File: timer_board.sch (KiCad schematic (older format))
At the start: 17 parts

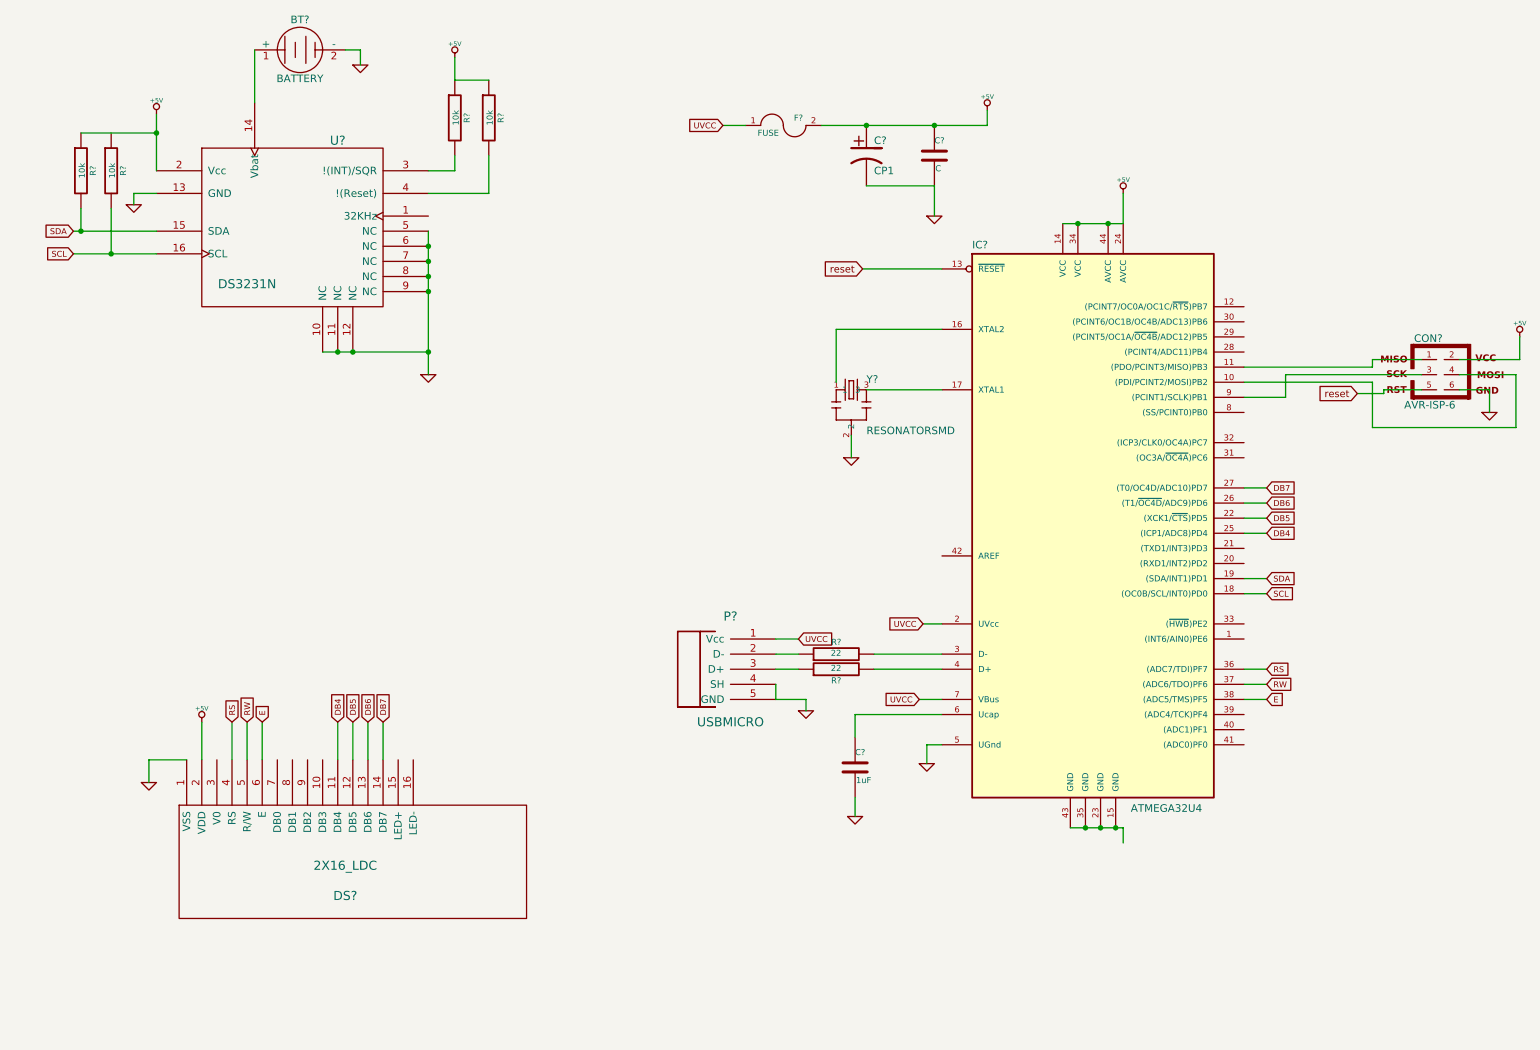
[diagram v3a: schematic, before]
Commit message: Added Relay
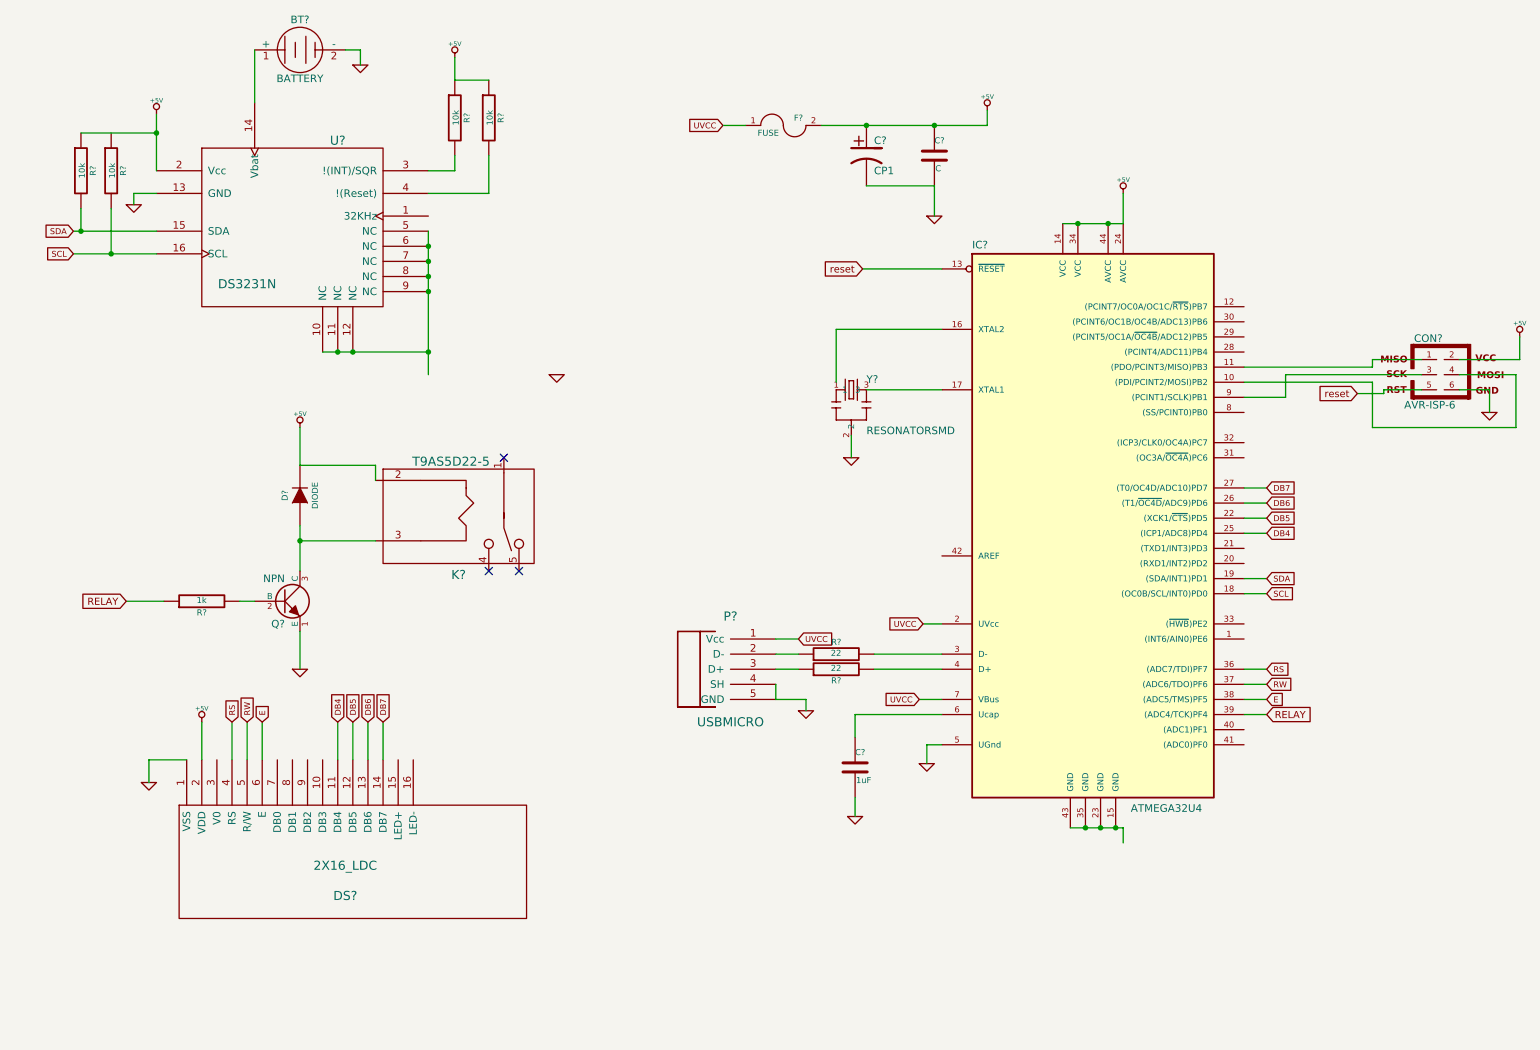
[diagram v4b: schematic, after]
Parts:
- added D?: DIODE, ~, symbol DIODE
- added K?: T9AS5D22-5, symbol T9AS5D22-5
- added Q?: NPN, ~, symbol NPN
- added R?: 1k, ~, symbol R
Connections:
- net +5V: now also D?.2 (K), K?.2
- net GND: now also Q?.1 (E); no longer U?.10 (NC), U?.11 (NC), U?.12 (NC), U?.5 (NC), U?.6 (NC), U?.7 (NC), U?.8 (NC), U?.9 (NC)
- net RELAY: now reaches IC?.39 ((ADC4/TCK)PF4)
- net RELAY: now also R?.1
- new net: U?.10 (NC), U?.11 (NC), U?.12 (NC), U?.5 (NC), U?.6 (NC), U?.7 (NC), U?.8 (NC), U?.9 (NC)
- new net: D?.1 (A), K?.3, Q?.3 (C)
- new net: Q?.2 (B), R?.2
- no-connect marks 0 -> 3
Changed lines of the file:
@@
-EESchema Schematic File Version 2  date 6/27/2013 10:57:25 PM
+EESchema Schematic File Version 2  date 6/30/2013 12:25:42 AM
 LIBS:power
 LIBS:device
@@
 LIBS:atmega32u4
 LIBS:custom_parts
-LIBS:Dispositivos_I2C
 LIBS:timer_board-cache
 EELAYER 27 0
@@
 Sheet 1 1
 Title ""
-Date "28 jun 2013"
+Date "30 jun 2013"
 Rev ""
 Comp ""
@@
 L GND #PWR?
 U 1 1 51C67EB1
-P 3300 2900
-F 0 "#PWR?" H 3300 2900 30  0001 C CNN
-F 1 "GND" H 3300 2830 30  0001 C CNN
-F 2 "" H 3300 2900 60  0000 C CNN
-F 3 "" H 3300 2900 60  0000 C CNN
-	1    3300 2900
+P 4150 2900
+F 0 "#PWR?" H 4150 2900 30  0001 C CNN
+F 1 "GND" H 4150 2830 30  0001 C CNN
+F 2 "" H 4150 2900 60  0000 C CNN
+F 3 "" H 4150 2900 60  0000 C CNN
+	1    4150 2900
 	1    0    0    -1
 $EndComp
@@
 Wire Wire Line
 	2850 750  2850 850
+$Comp
+L T9AS5D22-5 K?
+U 1 1 51CFD049
+P 3500 3750
+F 0 "K?" H 3500 3275 60  0000 C CNN
+F 1 "T9AS5D22-5" H 3450 4025 60  0000 C CNN
+F 2 "" H 3600 3750 60  0000 C CNN
+F 3 "" H 3600 3750 60  0000 C CNN
+	1    3500 3750
+	1    0    0    -1
+$EndComp
+$Comp
+L NPN Q?
+U 1 1 51CFD058
+P 2350 4400
+F 0 "Q?" H 2350 4250 50  0000 R CNN
+F 1 "NPN" H 2350 4550 50  0000 R CNN
+F 2 "~" H 2350 4400 60  0000 C CNN
+F 3 "~" H 2350 4400 60  0000 C CNN
+	1    2350 4400
+	1    0    0    -1
+$EndComp
+$Comp
+L GND #PWR?
+U 1 1 51CFD065
+P 2450 4850
+F 0 "#PWR?" H 2450 4850 30  0001 C CNN
+F 1 "GND" H 2450 4780 30  0001 C CNN
+F 2 "" H 2450 4850 60  0000 C CNN
+F 3 "" H 2450 4850 60  0000 C CNN
+	1    2450 4850
+	1    0    0    -1
+$EndComp
+Wire Wire Line
+	2450 4600 2450 4850
+Wire Wire Line
+	2450 3900 2450 4200
+Wire Wire Line
+	2450 4000 2950 4000
+$Comp
+L DIODE D?
+U 1 1 51CFD13D
+P 2450 3700
+F 0 "D?" H 2450 3800 40  0000 C CNN
+F 1 "DIODE" H 2450 3600 40  0000 C CNN
+F 2 "~" H 2450 3700 60  0000 C CNN
+F 3 "~" H 2450 3700 60  0000 C CNN
+	1    2450 3700
+	0    -1   -1   0
+$EndComp
+Connection ~ 2450 4000
+Wire Wire Line
+	2950 3600 2950 3500
+Wire Wire Line
+	2950 3500 2450 3500
+$Comp
+L +5V #PWR?
+U 1 1 51CFD28C
+P 2450 3250
+F 0 "#PWR?" H 2450 3340 20  0001 C CNN
+F 1 "+5V" H 2450 3340 30  0000 C CNN
+F 2 "" H 2450 3250 60  0000 C CNN
+F 3 "" H 2450 3250 60  0000 C CNN
+	1    2450 3250
+	1    0    0    -1
+$EndComp
+Wire Wire Line
+	2450 3500 2450 3250
+$Comp
+L R R?
+U 1 1 51CFD2FF
+P 1800 4400
+F 0 "R?" V 1725 4400 40  0000 C CNN
+F 1 "1k" V 1807 4401 40  0000 C CNN
+F 2 "~" V 1730 4400 30  0000 C CNN
+F 3 "~" H 1800 4400 30  0000 C CNN
+	1    1800 4400
+	0    -1   -1   0
+$EndComp
+Wire Wire Line
+	2050 4400 2150 4400
+Text GLabel 1300 4400 0    47   Input ~ 0
+RELAY
+Wire Wire Line
+	1300 4400 1550 4400
+Text GLabel 8850 5150 2    47   Input ~ 0
+RELAY
+Wire Wire Line
+	8850 5150 8700 5150
+NoConn ~ 3700 4200
+NoConn ~ 3900 4200
+NoConn ~ 3800 3450
 $EndSCHEMATC

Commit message: Added buttons
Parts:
- added C? (x5): 1uF, ~, symbol C
- added D?: LED, ~, symbol LED
- added Q?: NPN, ~, symbol NPN
- added R? (x5): 5k, ~, symbol R
- added R? (x2): 2.2k, ~, symbol R
- added S?: UP, ~, symbol RESET
- added S?: DOWN, ~, symbol RESET
- added S?: LEFT, ~, symbol RESET
- added S?: RIGHT, ~, symbol RESET
- added S?: SELECT, ~, symbol RESET
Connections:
- net labels added: BACK, Down, Left, Right, Select, UP
- wire segments 94 -> 134
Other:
- moved on the sheet: D?, DS?, K?, Q?, R?
